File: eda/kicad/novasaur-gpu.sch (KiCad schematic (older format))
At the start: 20 parts, among them U1 74F86, U2 74F08, U28 74F163, U29 74F163, U30 74F541, U31 74F574, U32 74F574, U33 74F541, U34 74F574, U35 74F299, U36 74F574, U37 74F157

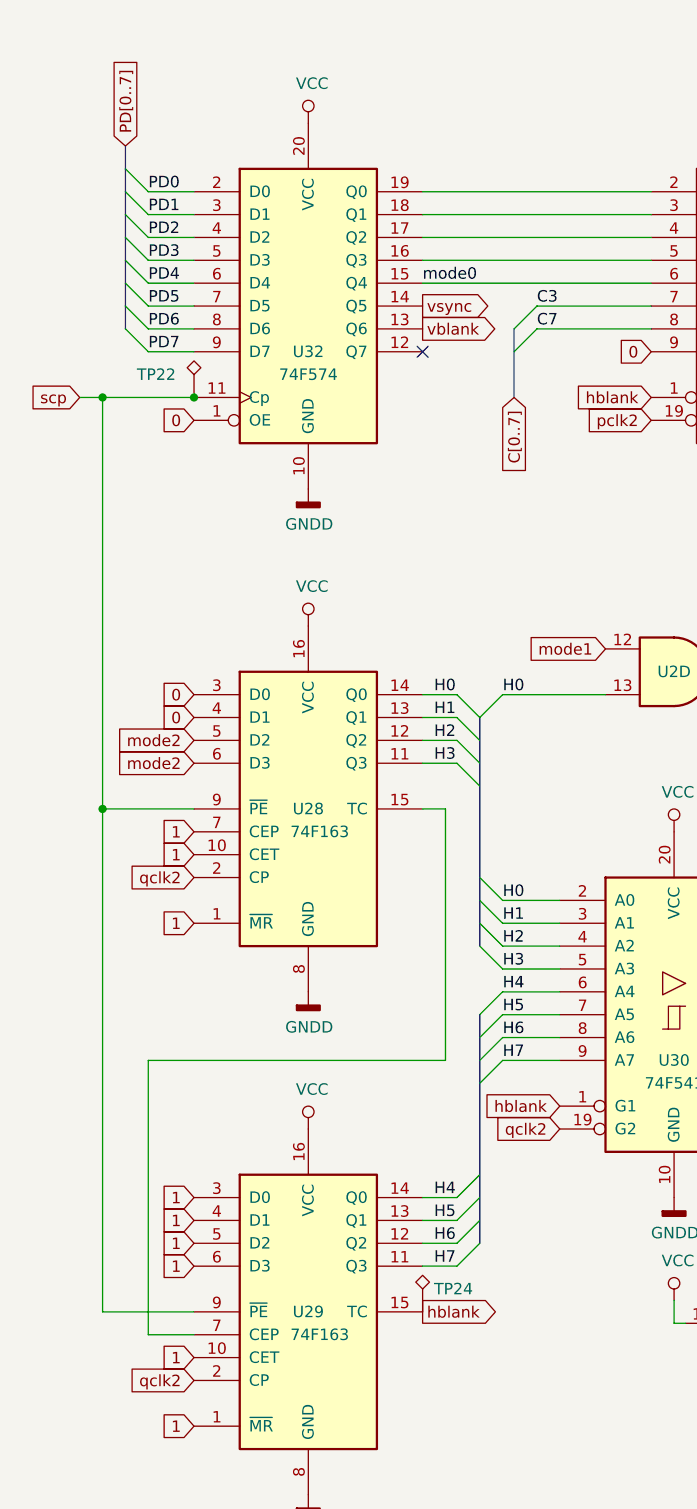
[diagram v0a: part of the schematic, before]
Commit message: build out, fix bugs Build out the initial HAL VM code to generate video timing. Not quite working yet, but lots of bugs fixed with assembler and code
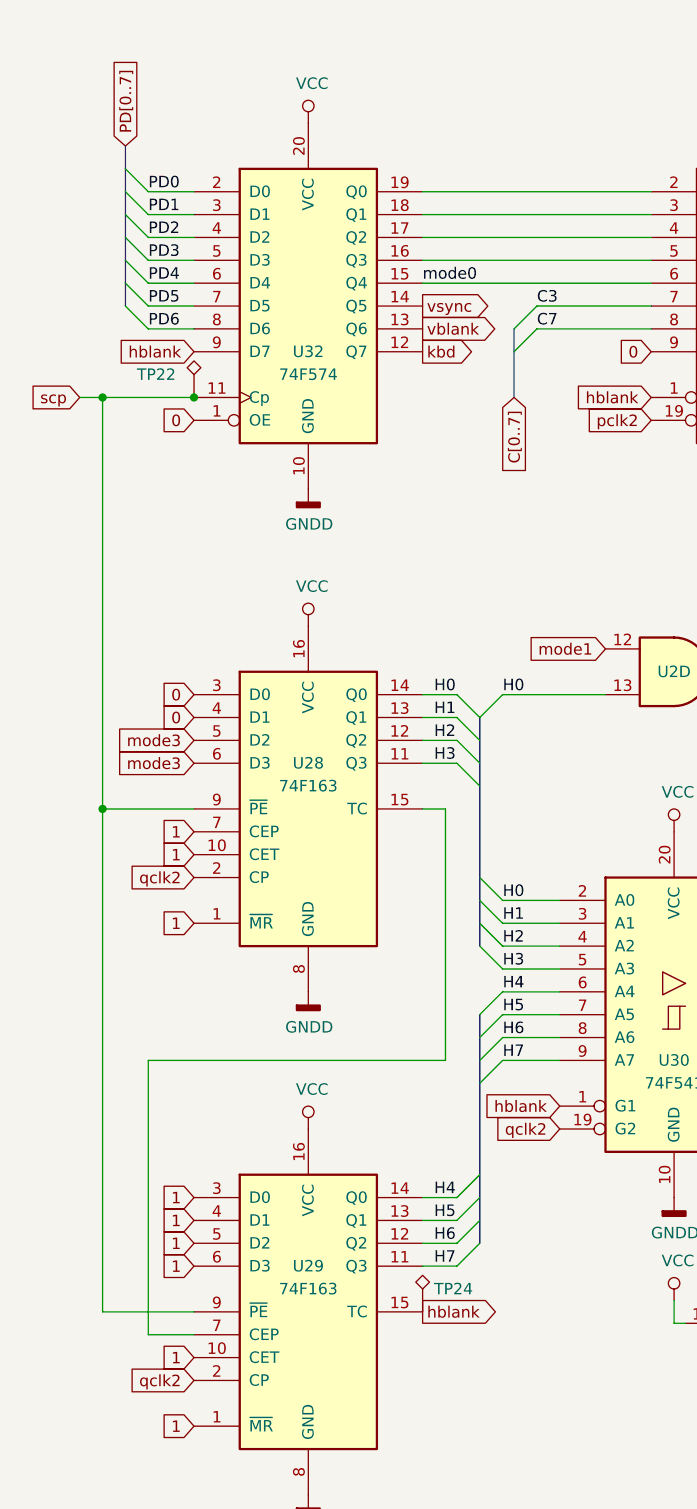
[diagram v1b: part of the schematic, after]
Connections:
- net mode2 is gone; now on net mode3: U28.5 (D2), U28.6 (D3)
- net PD7: no longer U32.9 (D7)
- net hblank: now also U32.9 (D7)
- net kbd: now reaches U32.12 (Q7)
- no-connect marks 3 -> 2
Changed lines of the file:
@@
 Sheet 3 4
 Title "GPU"
-Date "2020-02-15"
+Date "2020-02-20"
 Rev "1.5"
 Comp ""
@@
 AR Path="/5DAA5CD8/5D9A6C5F/5E4B79C3" Ref="U?"  Part="1"
 AR Path="/5DA1E9BD/5E4B79C3" Ref="U29"  Part="1"
-F 0 "U29" H 2150 6450 50  0000 C CNN
-F 1 "74F163" H 2200 6350 50  0000 C CNN
+F 0 "U29" H 2150 6650 50  0000 C CNN
+F 1 "74F163" H 2150 6550 50  0000 C CNN
 F 2 "Package_DIP:DIP-16_W7.62mm_LongPads" H 2150 6450 50  0001 C CNN
 F 3 "http://www.ti.com/lit/gpn/sn74LS163" H 2150 6450 50  0001 C CNN
@@
 0
 Text GLabel 1650 3950 0    50   Input ~ 0
-mode2
+mode3
 Text GLabel 1650 3750 0    50   Input ~ 0
 0
 Text GLabel 1650 4050 0    50   Input ~ 0
-mode2
+mode3
 Wire Wire Line
 	2650 4250 2750 4250
@@
 AR Path="/5DAA5CD8/5D9A6C5F/5E4B7483" Ref="U?"  Part="1"
 AR Path="/5DA1E9BD/5E4B7483" Ref="U28"  Part="1"
-F 0 "U28" H 2150 4250 50  0000 C CNN
-F 1 "74F163" H 2200 4150 50  0000 C CNN
+F 0 "U28" H 2150 4450 50  0000 C CNN
+F 1 "74F163" H 2150 4350 50  0000 C CNN
 F 2 "Package_DIP:DIP-16_W7.62mm_LongPads" H 2150 4250 50  0001 C CNN
 F 3 "http://www.ti.com/lit/gpn/sn74LS163" H 2150 4250 50  0001 C CNN
@@
 Wire Wire Line
 	1450 2150 1650 2150
-NoConn ~ 2650 2250
 $Comp
 L 74xx:74LS08 U?
@@
 $Comp
 L Connector:TestPoint_Alt TP?
-U 1 1 5E144DCF
-P 1650 2450
-AR Path="/5E144DCF" Ref="TP?"  Part="1"
-AR Path="/5DA1E9BA/5E144DCF" Ref="TP?"  Part="1"
-AR Path="/5DA1E9BD/5E144DCF" Ref="TP22"  Part="1"
-F 0 "TP22" H 1400 2550 50  0000 L CNN
-F 1 "SCP" H 1400 2600 50  0001 L CNN
-F 2 "TestPoint:TestPoint_Pad_1.0x1.0mm" H 1850 2450 50  0001 C CNN
-F 3 "~" H 1850 2450 50  0001 C CNN
-	1    1650 2450
-	1    0    0    -1
-$EndComp
-Connection ~ 1650 2450
-$Comp
-L Connector:TestPoint_Alt TP?
 U 1 1 5E19A64A
 P 2650 6450
@@
 Connection ~ 1250 2450
 Wire Wire Line
-	1250 2450 1650 2450
-Wire Wire Line
 	1250 4250 1250 6450
 Connection ~ 1250 4250
@@
 Wire Wire Line
 	9050 2450 9200 2450
-Text Label 1450 2250 0    50   ~ 0
-PD7
-Entry Wire Line
-	1450 2250 1350 2150
-Wire Wire Line
-	1450 2250 1650 2250
 Wire Wire Line
 	5700 3650 5900 3650
@@
 Text Label 2650 1950 0    50   ~ 0
 mode0
+Text GLabel 1650 2250 0    50   Input ~ 0
+hblank
+Text GLabel 2650 2250 2    50   Output ~ 0
+kbd
+Connection ~ 1650 2450
+Wire Wire Line
+	1250 2450 1650 2450
+$Comp
+L Connector:TestPoint_Alt TP?
+U 1 1 5E144DCF
+P 1650 2450
+AR Path="/5E144DCF" Ref="TP?"  Part="1"
+AR Path="/5DA1E9BA/5E144DCF" Ref="TP?"  Part="1"
+AR Path="/5DA1E9BD/5E144DCF" Ref="TP22"  Part="1"
+F 0 "TP22" H 1400 2550 50  0000 L CNN
+F 1 "SCP" H 1400 2600 50  0001 L CNN
+F 2 "TestPoint:TestPoint_Pad_1.0x1.0mm" H 1850 2450 50  0001 C CNN
+F 3 "~" H 1850 2450 50  0001 C CNN
+	1    1650 2450
+	1    0    0    -1
+$EndComp
 Wire Bus Line
 	3050 2150 3050 2450
+Wire Bus Line
+	1350 1350 1350 2050
 Wire Bus Line
 	2900 3850 2900 4850
@@
 	6350 4750 6350 5650
 Wire Bus Line
-	1350 1350 1350 2150
-Wire Bus Line
 	7850 4750 7850 5550

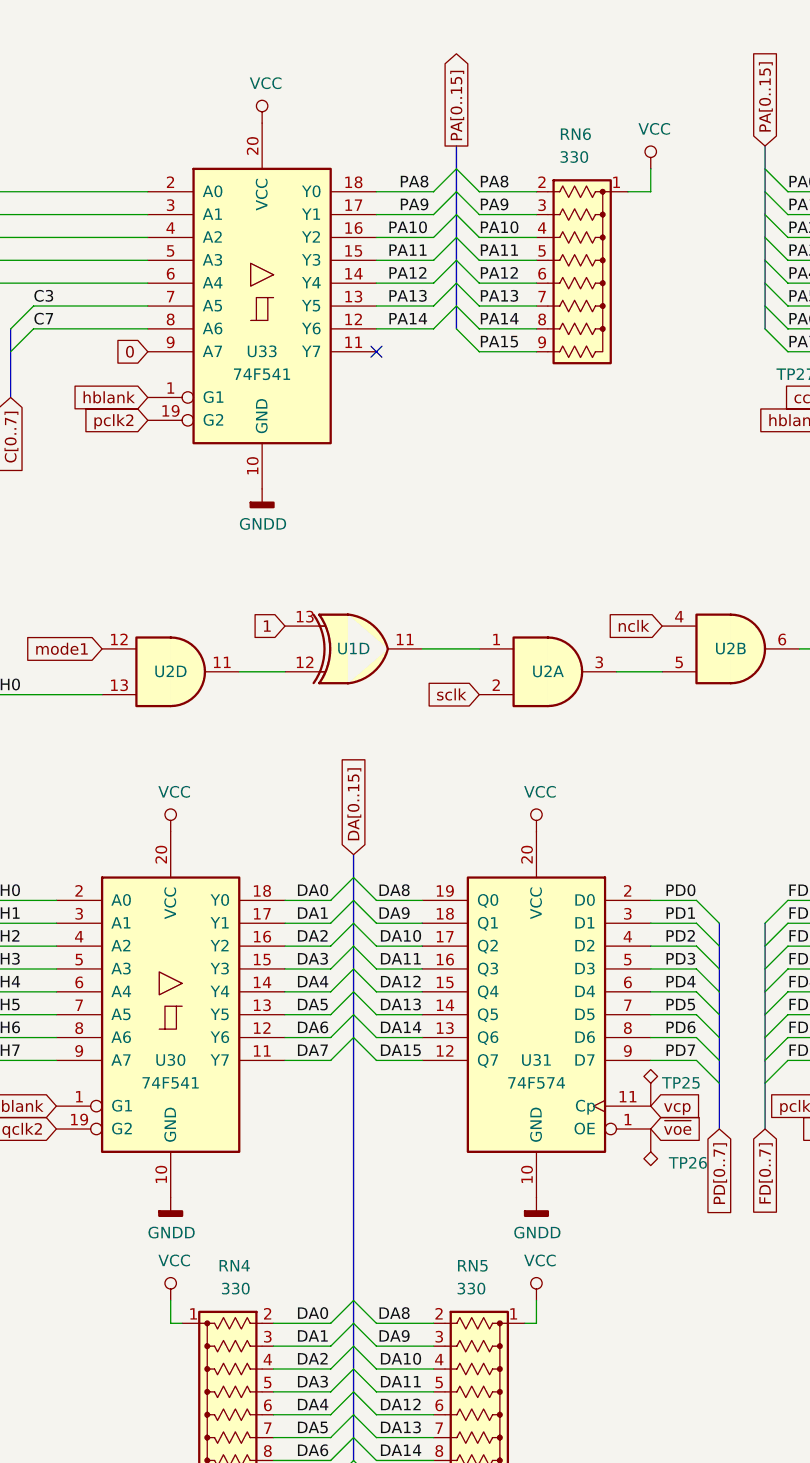
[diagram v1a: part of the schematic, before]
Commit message: final rev5 update before removing buck reg
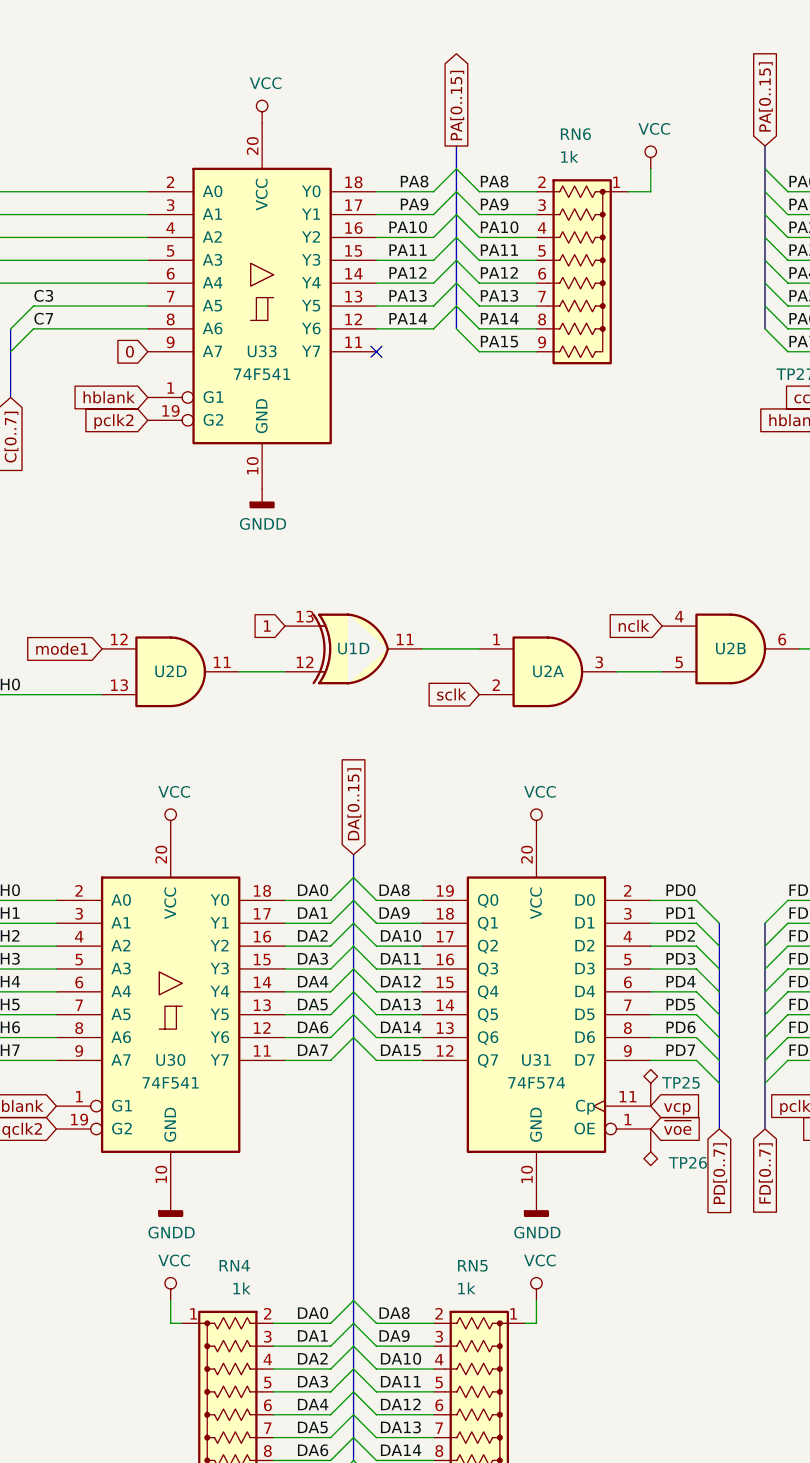
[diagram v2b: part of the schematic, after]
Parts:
- RN2, RN3, RN4: value 330 -> 1k
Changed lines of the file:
@@
 AR Path="/5DA1E9BD/5D1C9541" Ref="RN6"  Part="1"
 F 0 "RN6" V 4900 1850 50  0000 L CNN
-F 1 "330" V 5000 1850 50  0000 L CNN
+F 1 "1k" V 5000 1850 50  0000 L CNN
 F 2 "Resistor_THT:R_Array_SIP9" V 6025 1950 50  0001 C CNN
 F 3 "http://www.vishay.com/docs/31509/csc.pdf" H 5550 1950 50  0001 C CNN
@@
 AR Path="/5DA1E9BD/5D1C1190" Ref="RN5"  Part="1"
 F 0 "RN5" V 4450 6800 50  0000 L CNN
-F 1 "330" V 4550 6800 50  0000 L CNN
+F 1 "1k" V 4550 6800 50  0000 L CNN
 F 2 "Resistor_THT:R_Array_SIP9" V 5575 6900 50  0001 C CNN
 F 3 "http://www.vishay.com/docs/31509/csc.pdf" H 5100 6900 50  0001 C CNN
@@
 AR Path="/5DA1E9BD/5D1C1196" Ref="RN4"  Part="1"
 F 0 "RN4" V 3350 6800 50  0000 L CNN
-F 1 "330" V 3450 6800 50  0000 L CNN
+F 1 "1k" V 3450 6800 50  0000 L CNN
 F 2 "Resistor_THT:R_Array_SIP9" V 4475 6900 50  0001 C CNN
 F 3 "http://www.vishay.com/docs/31509/csc.pdf" H 4000 6900 50  0001 C CNN

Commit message: power sw + super caps
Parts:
- TP27: value CCP -> TCP
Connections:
- net C0 renamed T0
- net C1 renamed T1
- net C2 renamed T2
- net C3 renamed T3
- net C4 renamed T4
- net C5 renamed T5
- net C6 renamed T6
- net C7 renamed T7
- net ccp renamed tcp
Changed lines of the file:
@@
 Sheet 3 4
 Title "Novasaur Retrocomputer"
-Date "2020-03-31"
+Date "2020-05-02"
 Rev "1.6"
 Comp ""
@@
 vsync
 Text GLabel 3050 2450 3    50   Input ~ 0
-C[0..7]
+T[0..7]
 Entry Wire Line
 	3050 2150 3150 2050
 Text Label 3150 2050 0    50   ~ 0
-C3
+T3
 Entry Wire Line
 	3050 2250 3150 2150
 Text Label 3150 2150 0    50   ~ 0
-C7
+T7
 Text Label 1450 1550 0    50   ~ 0
 PD0
@@
 r
 Text GLabel 6650 2450 0    50   Input ~ 0
-ccp
+tcp
 Text GLabel 7850 1350 1    50   Output ~ 0
-C[0..7]
+T[0..7]
 Wire Wire Line
 	7950 2250 8050 2250
@@
 	6450 1550 6350 1450
 Text Label 7650 2050 0    50   ~ 0
-C5
+T5
 Text Label 7950 2250 0    50   ~ 0
-C6
+T6
 Text Label 7950 2150 0    50   ~ 0
-C2
+T2
 Text Label 7950 1950 0    50   ~ 0
-C5
+T5
 Text Label 7950 1850 0    50   ~ 0
-C1
+T1
 Text Label 7950 1650 0    50   ~ 0
-C4
+T4
 Text Label 7950 1550 0    50   ~ 0
-C0
+T0
 Text Label 7650 2250 0    50   ~ 0
-C7
+T7
 Text Label 7650 2150 0    50   ~ 0
-C6
+T6
 Text Label 7650 1950 0    50   ~ 0
-C4
+T4
 Text Label 7650 1850 0    50   ~ 0
-C3
+T3
 Text Label 7650 1750 0    50   ~ 0
-C2
+T2
 Text Label 7650 1650 0    50   ~ 0
-C1
+T1
 Text Label 7650 1550 0    50   ~ 0
-C0
+T0
 Entry Wire Line
 	7850 2150 7750 2250
@@
 AR Path="/5DA1E9BD/5E199218" Ref="TP27"  Part="1"
 F 0 "TP27" H 6400 2550 50  0000 L CNN
-F 1 "CCP" H 6400 2600 50  0001 L CNN
+F 1 "TCP" H 6400 2600 50  0001 L CNN
 F 2 "TestPoint:TestPoint_Pad_1.0x1.0mm" H 6850 2450 50  0001 C CNN
 F 3 "~" H 6850 2450 50  0001 C CNN
